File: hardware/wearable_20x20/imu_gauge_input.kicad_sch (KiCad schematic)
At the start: 11 parts, among them U20 BMI270, U21 MAX17048G+T10

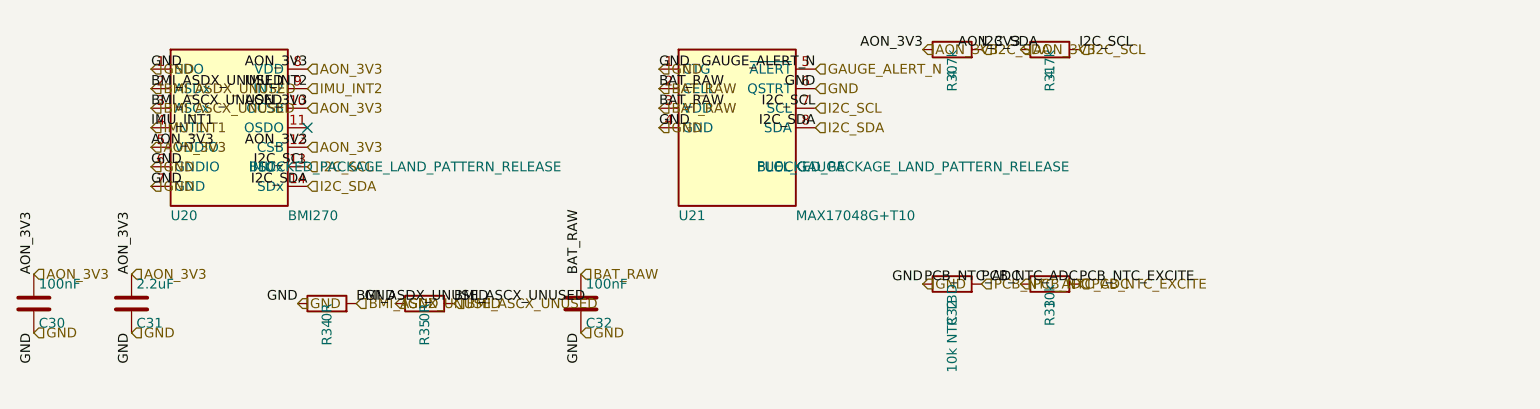
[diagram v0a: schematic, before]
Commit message: Release verified charger and sensor footprints
Co-authored-by: illiapliukhin <illiapliukhin@users.noreply.github.com>
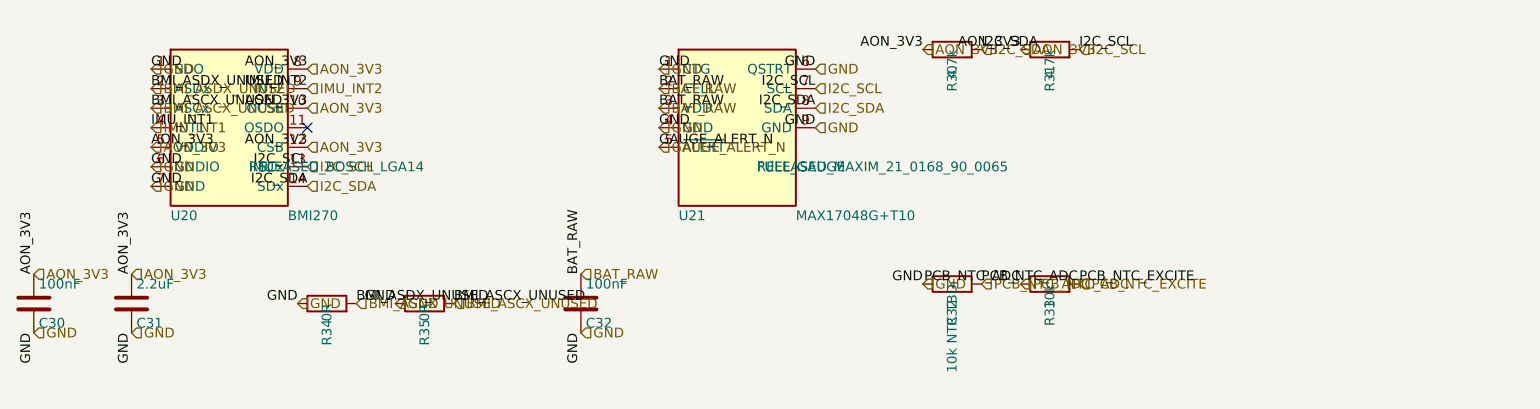
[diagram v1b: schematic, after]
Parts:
- U20: footprint (none) -> Package_LGA:Bosch_LGA-14_3x2.5mm_P0.5mm; FootprintStatus BLOCKED_PACKAGE_LAND_PATTERN_RELEASE -> RELEASED_BOSCH_LGA14
- U21: footprint (none) -> Package_DFN_QFN:TDFN-8-1EP_2x2mm_P0.5mm_EP0.8x1.2mm; FootprintStatus BLOCKED_PACKAGE_LAND_PATTERN_RELEASE -> RELEASED_MAXIM_21_0168_90_0065
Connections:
- net GND: now also U21.9 (GND)

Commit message: Regenerate hierarchies with selected EVT parts
Co-authored-by: illiapliukhin <illiapliukhin@users.noreply.github.com>
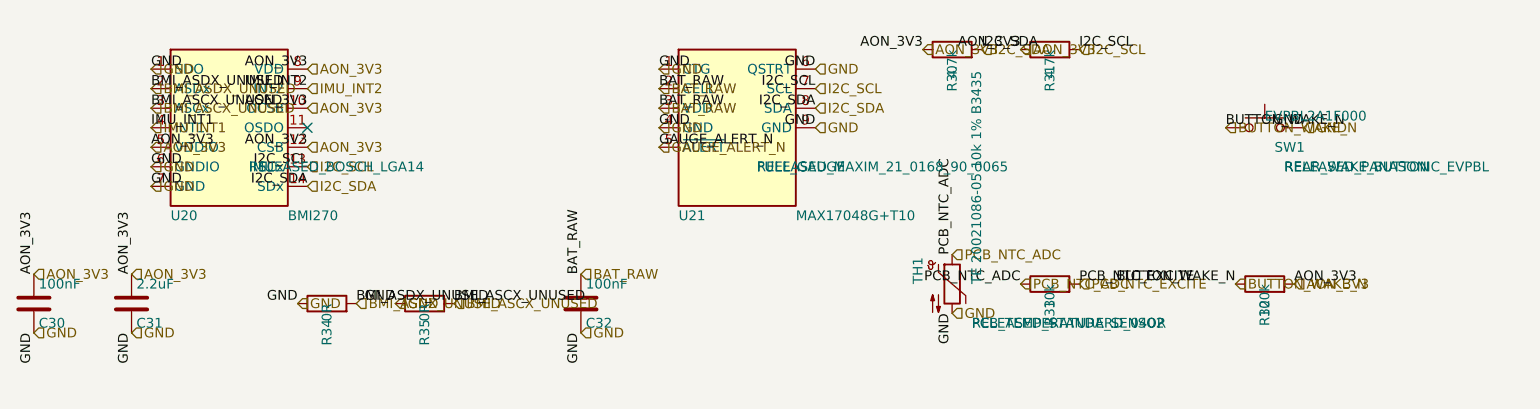
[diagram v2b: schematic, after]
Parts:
- added SW1: EVPBL2A1F000, PartSignal_Packages:Panasonic_EVPBL2A1F000_Switch, symbol Switch:SW_Push
- added TH1: TE 20021086-05 10k 1% B3435, Resistor_SMD:R_0402_1005Metric, symbol Device:Thermistor_NTC
- R32: value 10k NTC TBD -> 100k
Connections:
- net AON_3V3: now also R32.2
- net GND: now also SW1.2, TH1.2; no longer R32.1
- net PCB_NTC_ADC: now also TH1.1; no longer R32.2
- new net BUTTON_WAKE_N: R32.1, SW1.1
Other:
- moved on the sheet: R32
